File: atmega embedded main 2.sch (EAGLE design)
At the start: 146 parts, among them IC1 ATMEGA328PROUND, K1 SWITCH, K100 SWITCH, K101 SWITCH, K102 SWITCH, K103 SWITCH, K104 SWITCH, K105 SWITCH, K106 SWITCH, K107 SWITCH, K108 SWITCH, K109 SWITCH, K110 SWITCH, K111 SWITCH, K112 SWITCH, K113 SWITCH, K114 SWITCH, K115 SWITCH, K116 SWITCH, K117 SWITCH, K118 SWITCH, K119 SWITCH, K120 SWITCH, K121 SWITCH, K122 SWITCH, K123 SWITCH, K125 SWITCH, K126 SWITCH, K127 SWITCH, K128 SWITCH, K129 SWITCH, K130 SWITCH, K2 SWITCH, K3 SWITCH, K60 SWITCH, K67 SWITCH, K68 SWITCH, K69 SWITCH, K70 SWITCH, K71 SWITCH, K72 SWITCH, K73 SWITCH, K74 SWITCH, K75 SWITCH, K76 SWITCH, K77 SWITCH, K78 SWITCH, K79 SWITCH, K80 SWITCH, K81 SWITCH, K82 SWITCH, K83 SWITCH, K84 SWITCH, K85 SWITCH, K86 SWITCH, K87 SWITCH, K88 SWITCH, K89 SWITCH, K90 SWITCH, K91 SWITCH, K92 SWITCH, K93 SWITCH, K94 SWITCH, K95 SWITCH, K96 SWITCH, K98 SWITCH, K99 SWITCH

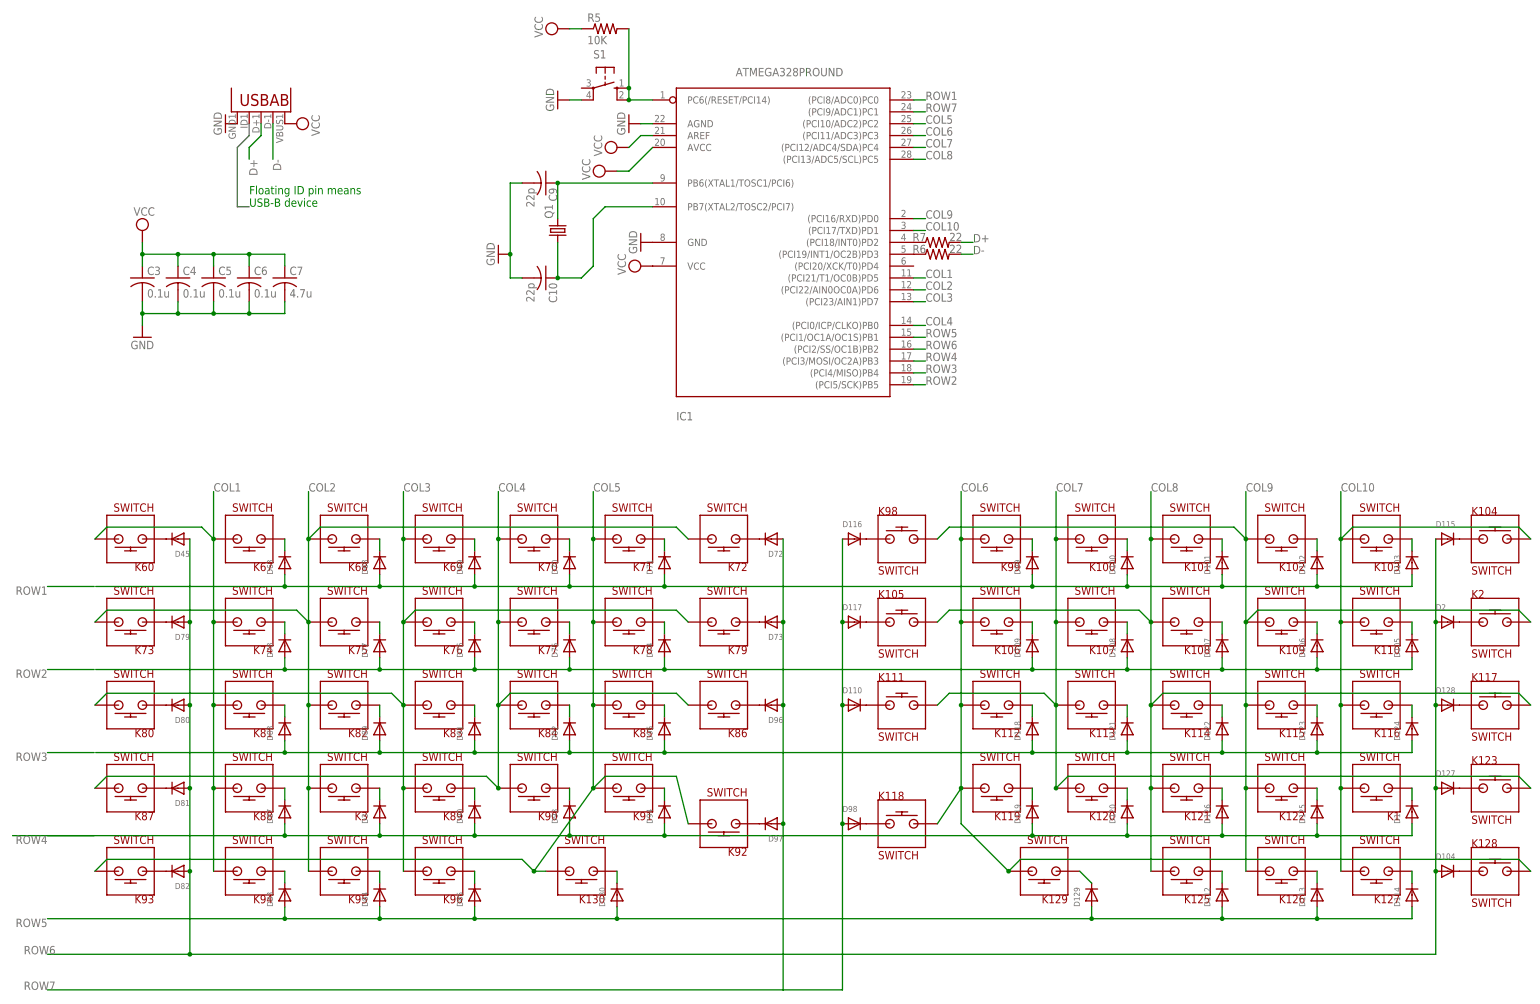
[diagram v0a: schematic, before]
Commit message: Fixed errors and made adjustments for USB
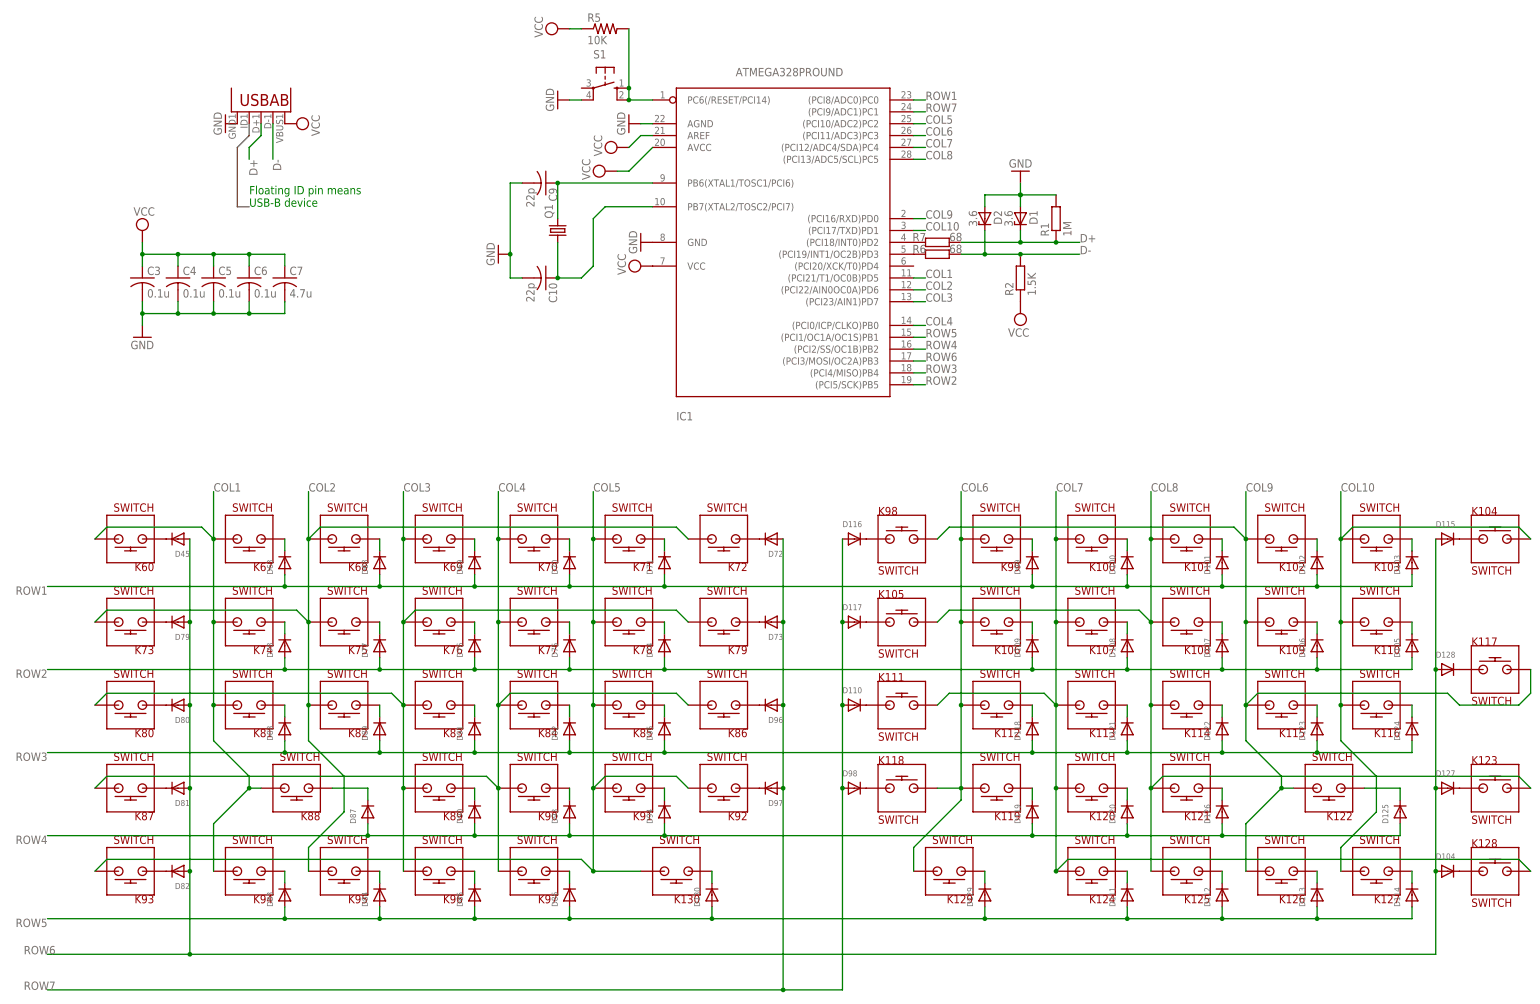
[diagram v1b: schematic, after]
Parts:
- removed D3: (no value), adafruit:DIODESMA
- removed K1, K2, K3: SWITCH, keyboard_switch:SWITCH
- added D111, D86: (no value), adafruit:DIODESMA
- added K124, K97: SWITCH, keyboard_switch:SWITCH
- added R1: 1M, eagle-ltspice:RR1206
- added R2: 1.5K, eagle-ltspice:RR1206
- D1, D2: value (none) -> 3.6; device adafruit:DIODESMA -> diode:ZENER-DIODESMB
- R6, R7: value 22 -> 68; device adafruit:R-US_M0805 -> eagle-ltspice:RR1206
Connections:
- removed net N$69: D1.C, K1.P$1
- net COL10: no longer K1.P$2
- net COL2: no longer K3.P$2
- net COL4: now also K97.P$2
- net COL6: no longer K128.P$2
- net COL7: now also K124.P$2, K128.P$2; no longer K123.P$2
- net COL8: now also K123.P$2; no longer K117.P$2
- net COL9: now also K117.P$2; no longer K2.P$2
- net D+: now also D1.C, R1.1
- net D-: now also D2.C, R2.2
- net GND: now also D1.A, D2.A, R1.2
- net N$23: now also D86.C, K97.P$1; no longer D3.C, K3.P$1
- net N$47: now also D111.C, K124.P$1; no longer D2.C, K2.P$1
- net ROW4: now also IC1.(PCI2/SS/OC1B)PB2; no longer D1.A, D3.A, IC1.(PCI3/MOSI/OC2A)PB3
- net ROW5: now also D111.A, D86.A
- net ROW6: now also IC1.(PCI3/MOSI/OC2A)PB3; no longer D2.A, IC1.(PCI2/SS/OC1B)PB2
- net VCC: now also R2.1
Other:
- moved on the sheet: D125, D128, D129, D130, D87, D97, D98, K117, K118, K122, K129, K130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
